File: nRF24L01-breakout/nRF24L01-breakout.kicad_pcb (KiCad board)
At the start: 2 copper layers, 41 x 17.6 mm, 20 parts, among them J1 Conn_01x08_Female, U1 NRF24L01, U2 Antenna_PCB_2.4GHz_50Ohm, Y1 Crystal_GND24_Small

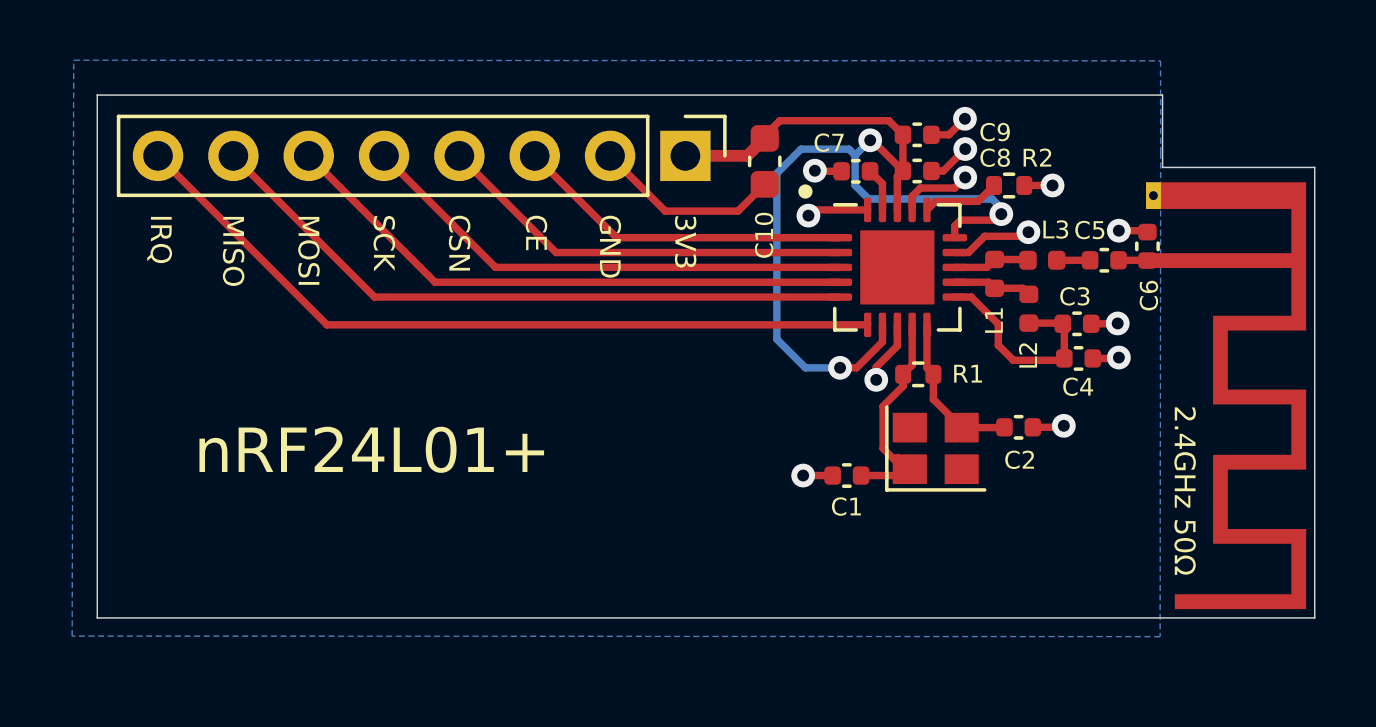
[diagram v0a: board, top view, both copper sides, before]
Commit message: Use Johanson 2450BM14A0002 matched balun
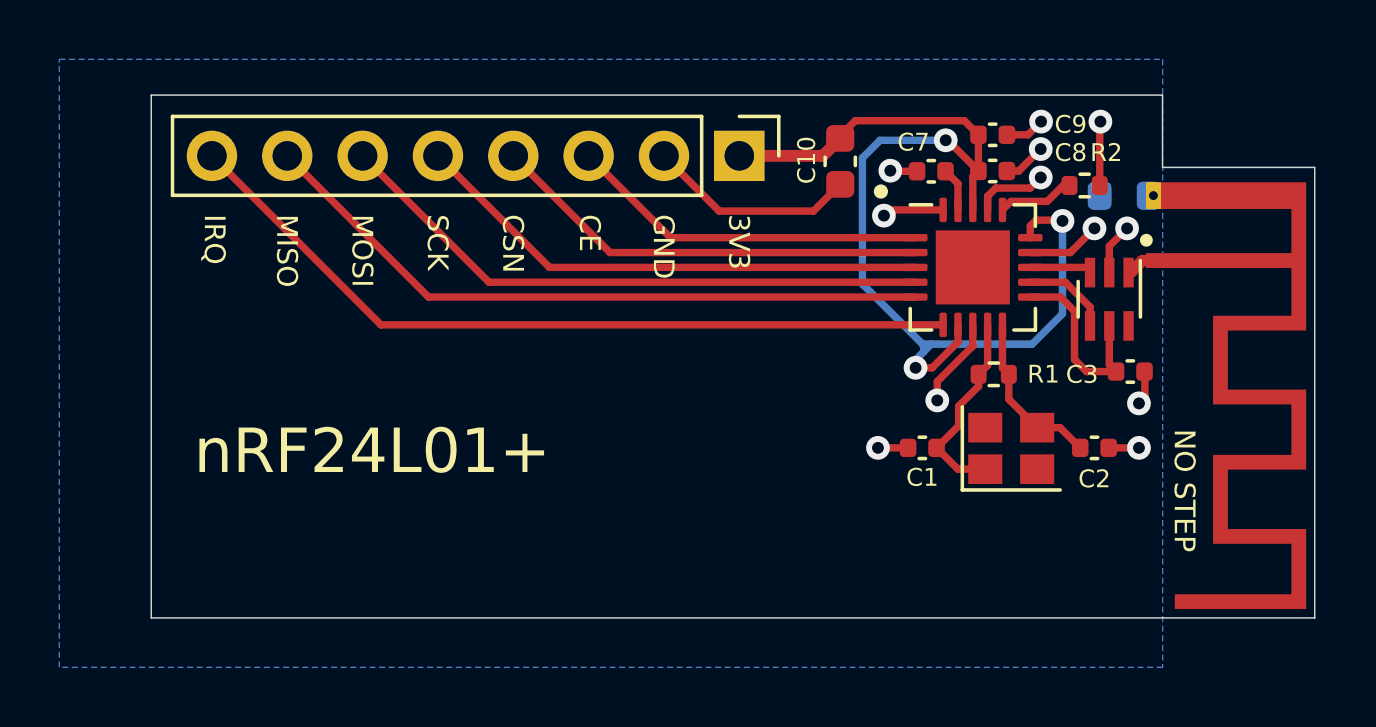
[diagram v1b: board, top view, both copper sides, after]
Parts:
- removed C4: 2.2nF, Capacitor_SMD:C_0402_1005Metric
- removed C5: 1.5pF, Capacitor_SMD:C_0402_1005Metric
- removed C6: 1pF, Capacitor_SMD:C_0402_1005Metric
- removed L1: 8.2nH, Inductor_SMD:L_0402_1005Metric
- removed L2: 2.7nH, Inductor_SMD:L_0402_1005Metric
- removed L3: 3.9nH, Inductor_SMD:L_0402_1005Metric
- added R3: 0k, Resistor_SMD:R_0603_1608Metric, B.Cu at (174.1, 87.3)
- added U3: Balun_2450BM14A0002, RF_Converter:Balun_Johanson_0896BM15A0001, F.Cu at (173.6, 90.8)
- moved C1 2.71 mm to (167.3, 95.8)
- moved C2 2.65 mm to (173.1, 95.8)
- moved R1 2.55 mm to (169.7, 93.3)
- moved R2 2.55 mm to (172.7, 86.9)
- moved U1 2.55 mm to (169.0, 89.7)
- moved Y1 2.55 mm to (170.3, 95.8)
- moved C10 2.54 mm to (164.5, 86.1)
- moved C7 2.54 mm to (167.6, 86.4)
- moved C8 2.54 mm to (169.6, 86.4)
- moved C9 2.54 mm to (169.6, 85.2)
- moved C3 2.41 mm to (174.3, 93.2)
- moved J1 1.82 mm to (161.1, 85.9)
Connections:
- net +3V3 renamed VDD
- U2 pad 2: GND -> Net-(U2-Pad2)
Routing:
- net GND: track 25.4 -> 28.0 mm, vias 13 -> 12
- net Net-(U2-Pad1): track 1.04 -> 3.31 mm
- net VDD: track 35.1 -> 36.6 mm
- net XC2: track 8.05 -> 6.80 mm
- net Net-(C5-Pad1): track 1.12 -> 0.00 mm
- net VDD_PA: track 7.36 -> 6.52 mm
- net SCK: track 16.9 -> 17.7 mm
- net IRQ: track 26.3 -> 27.0 mm
- net CE: track 11.4 -> 12.2 mm
- net MOSI: track 19.7 -> 20.4 mm
- net MISO: track 22.4 -> 23.1 mm
- net CSN: track 14.2 -> 14.9 mm
- net ANT2: track 2.59 -> 1.99 mm
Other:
- board size 41 x 17.6 mm -> 39.2 x 17.6 mm
- board text added: "NO STEP"
- board text removed: "2.4GHz 50Ω"

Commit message: Fix balun footprint; Make board smaller
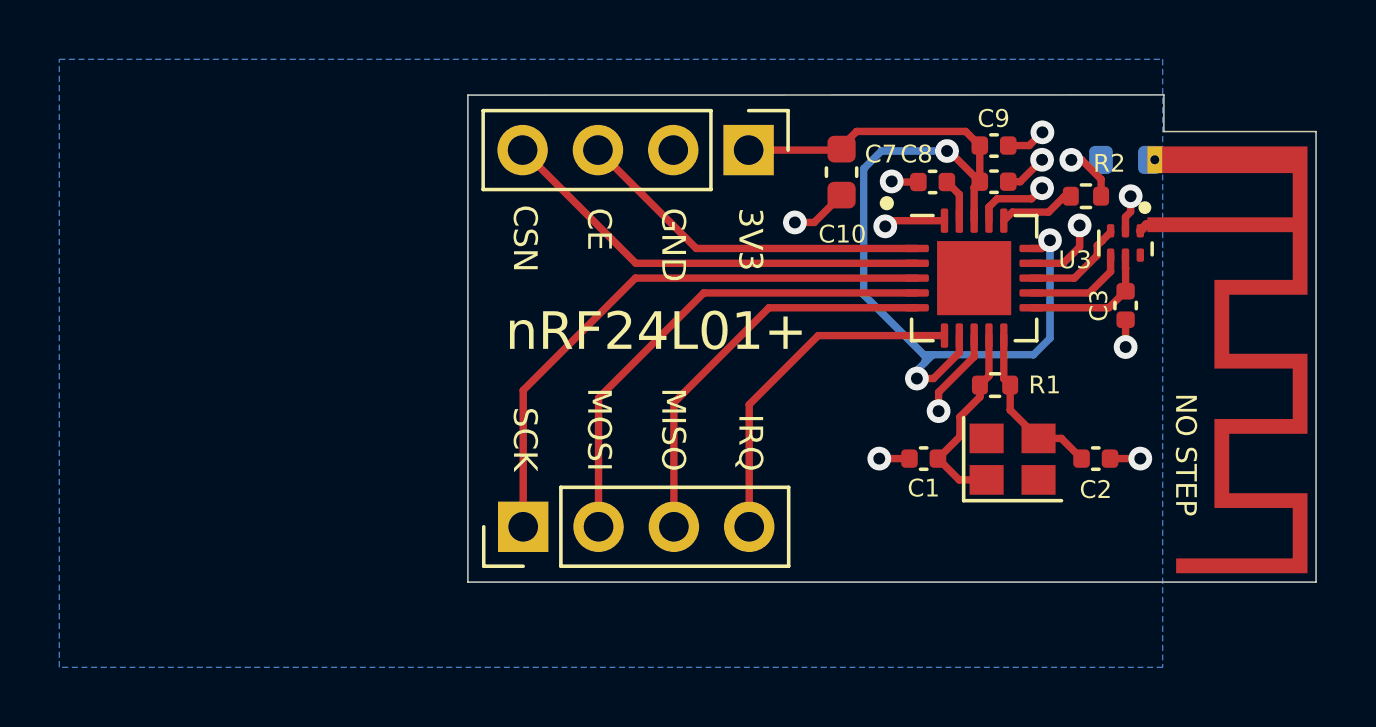
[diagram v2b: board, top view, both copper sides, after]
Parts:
- added J2: Conn_01x04_Female, Connector_PinHeader_2.54mm:PinHeader_1x04_P2.54mm_Vertical, F.Cu at (153.8, 98.4)
- J1: value Conn_01x08_Female -> Conn_01x04_Female; footprint Connector_PinHeader_2.54mm:PinHeader_1x08_P2.54mm_Vertical -> Connector_PinHeader_2.54mm:PinHeader_1x04_P2.54mm_Vertical
- U3: footprint RF_Converter:Balun_Johanson_0896BM15A0001 -> RF_Converter:Balun_Johanson_1.6x0.8mm
- moved C3 2.23 mm to (174.1, 91.0), turned to -90 degrees
- moved U3 1.97 mm to (174.1, 88.9)
- moved G*** 1.21 mm to (177.8, 92.4)
- moved R3 1.21 mm to (174.1, 86.1)
- moved U2 1.21 mm to (175.3, 88.0)
- moved J1 0.37 mm to (161.4, 85.7)
- moved C10 0.36 mm to (164.5, 86.5)
- moved C7 0.36 mm to (167.6, 86.8)
- moved C9 0.36 mm to (169.7, 85.6)
- moved C1 0.36 mm to (167.3, 96.1)
- moved C2 0.36 mm to (173.1, 96.1)
- moved R1 0.36 mm to (169.7, 93.6)
- moved R2 0.36 mm to (172.8, 87.3)
- moved Y1 0.36 mm to (170.3, 96.1)
- moved C8 0.36 mm to (169.7, 86.8)
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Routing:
- net IRQ: track 27.0 -> 11.7 mm
- net MISO: track 23.1 -> 13.7 mm
- net GND: track 28.0 -> 21.9 mm, vias 12 -> 13
- net MOSI: track 20.4 -> 16.5 mm
- net VDD_PA: track 6.52 -> 4.62 mm
- net VDD: track 36.6 -> 34.8 mm
- net SCK: track 17.7 -> 19.4 mm
- net ANT2: track 1.99 -> 3.55 mm
- net Net-(U2-Pad1): track 3.31 -> 2.79 mm
- net ANT1: track 3.00 -> 3.52 mm
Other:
- board size 39.2 x 17.6 mm -> 28.6 x 16.4 mm
